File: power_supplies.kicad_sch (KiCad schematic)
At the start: 47 parts, among them IC1 ECP5-BGA256, U15 1V8REG, U3 3V3REG, U4 1V15REG, U5 2V5REG

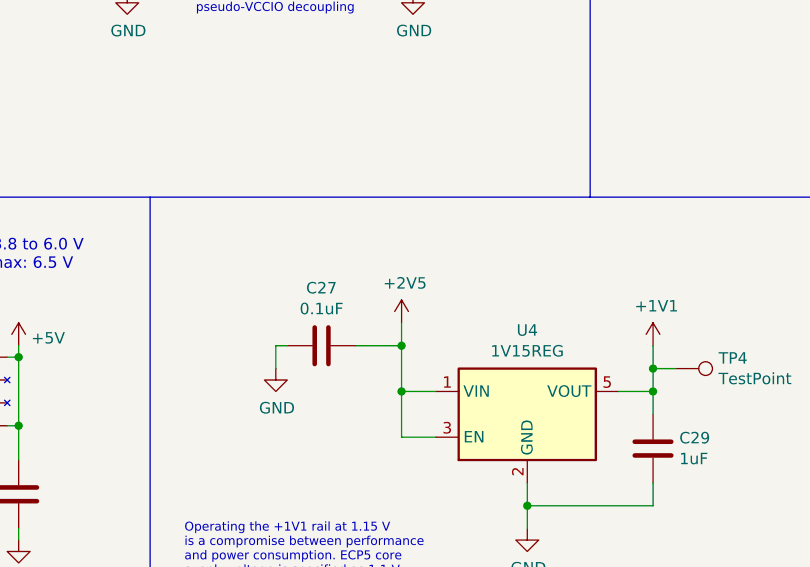
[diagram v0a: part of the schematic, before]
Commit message: Connect U4 +1V1 regulator input to +3V3, not +2V5
The FPGA can drive outputs unexpectedly during power supply ramp-up and
ramp-down. The +2V5 regulator starts abruptly when +3V3 approaches 2 V
and starts more slowly with +1V1 chained from it. With +1V1 chained from
+3V3 instead of from +2V5, both +1V1 and +2V5 supplies start up faster,
minimizing the duration of FPGA output glitches. This reduces the
duration of the glitch that causes #9.
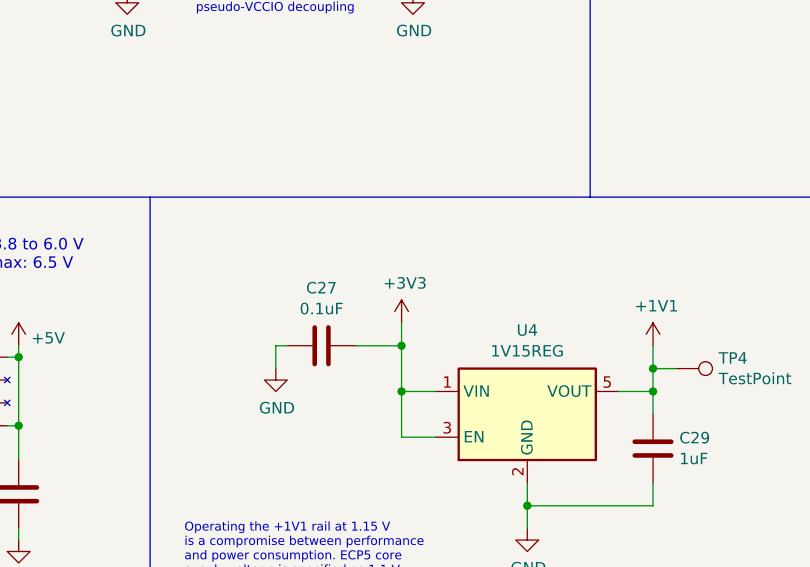
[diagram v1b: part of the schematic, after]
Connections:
- net +2V5: no longer C27.1, U4.1 (VIN), U4.3 (EN)
- net +3V3: now also C27.1, U4.1 (VIN), U4.3 (EN)
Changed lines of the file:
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@@
     (pin "2")
-  )
-  (symbol (lib_id "power:+2V5") (at 121.92 92.71 0) (unit 1)
-    (in_bom yes) (on_board yes)
-    (property "Reference" "#PWR030" (id 0) (at 121.92 96.52 0)
-      (effects (font (size 1.27 1.27)) hide)
-    )
-    (property "Value" "+2V5" (id 1) (at 122.301 88.3158 0))
-    (property "Footprint" "" (id 2) (at 121.92 92.71 0)
-      (effects (font (size 1.27 1.27)) hide)
-    )
-    (property "Datasheet" "" (id 3) (at 121.92 92.71 0)
-      (effects (font (size 1.27 1.27)) hide)
-    )
-    (pin "1")
   )
   (symbol (lib_id "power:+1V1") (at 149.86 95.25 0) (unit 1)
@@
     (pin "2")
   )
+  (symbol (lib_id "power:+3V3") (at 121.92 92.71 0) (unit 1)
+    (in_bom yes) (on_board yes)
+    (property "Reference" "#PWR030" (id 0) (at 121.92 96.52 0)
+      (effects (font (size 1.27 1.27)) hide)
+    )
+    (property "Value" "+3V3" (id 1) (at 122.301 88.3158 0))
+    (property "Footprint" "" (id 2) (at 121.92 92.71 0)
+      (effects (font (size 1.27 1.27)) hide)
+    )
+    (property "Datasheet" "" (id 3) (at 121.92 92.71 0)
+      (effects (font (size 1.27 1.27)) hide)
+    )
+    (pin "1")
+  )
   (symbol (lib_id "Device:R") (at 55.245 149.86 90) (unit 1)

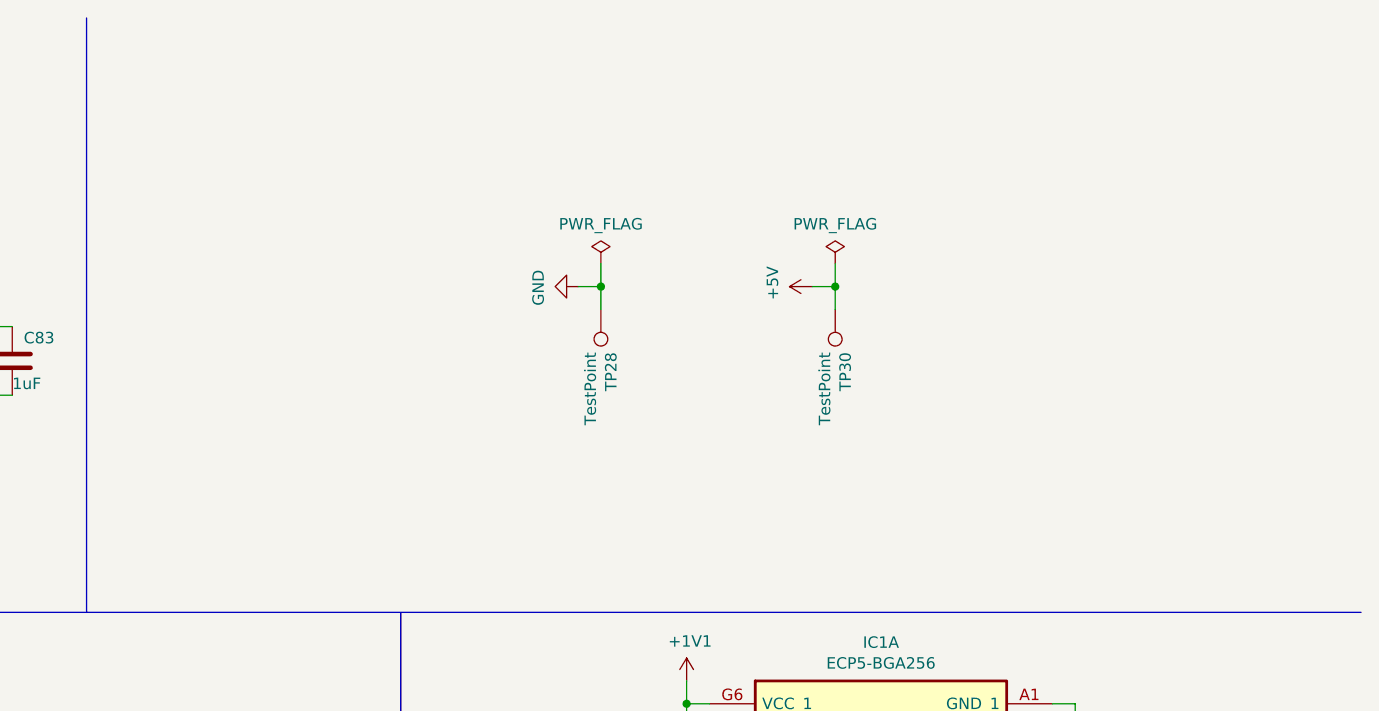
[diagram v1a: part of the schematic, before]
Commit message: Add POWER_GOOD signal
This open collector signal is driven low to indicate that +3V3 is at a
voltage high enough for the FPGA to operate normally. It is used to gate
power input and power passthrough control outputs from the FPGA.

Fixes #9
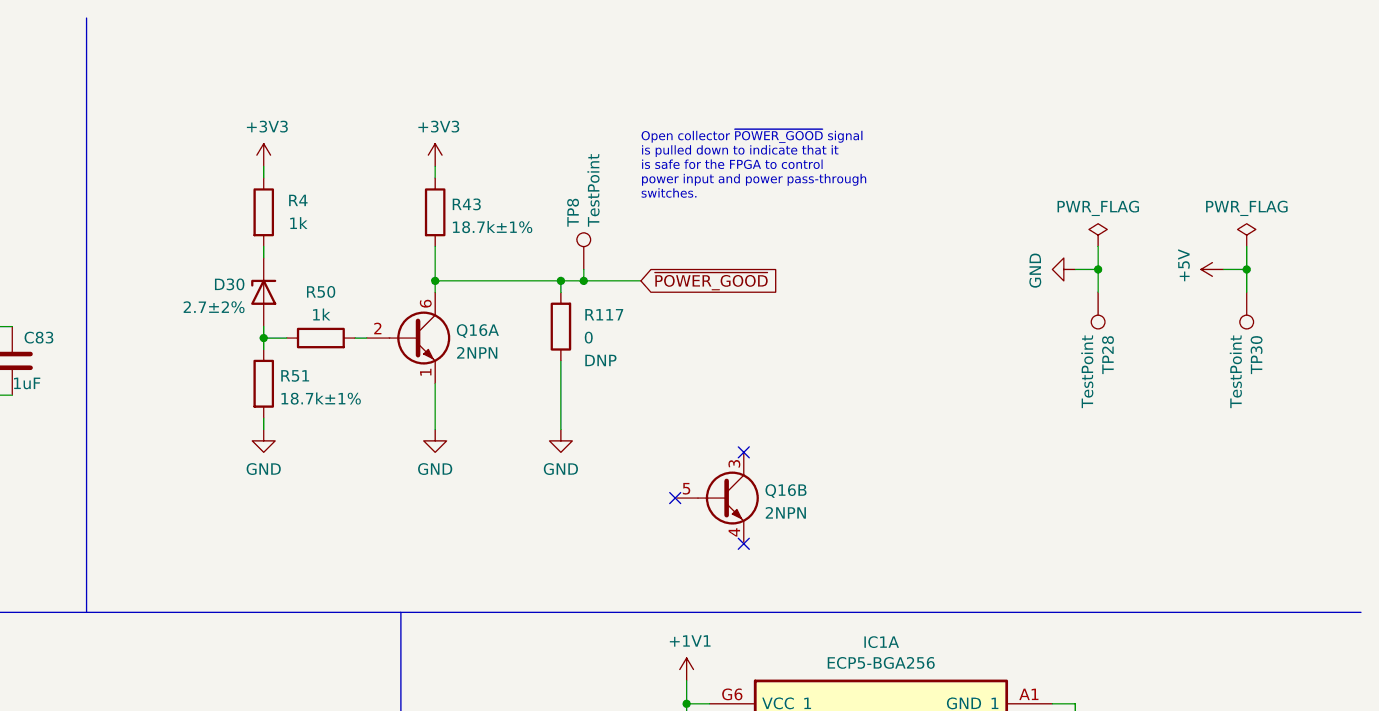
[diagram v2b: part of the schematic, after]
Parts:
- added D30: 2.7±2%, cynthion:DFN1006-2, symbol Device:D_Zener
- added Q16: 2NPN, Package_TO_SOT_SMD:SOT-363_SC-70-6, symbol Transistor_BJT:BC847BS
- added R117: 0, Resistor_SMD:R_0402_1005Metric, symbol Device:R
- added R4, R50: 1k, Resistor_SMD:R_0402_1005Metric, symbol Device:R
- added R43, R51: 18.7k±1%, Resistor_SMD:R_0402_1005Metric, symbol Device:R
- added TP8: TestPoint, TestPoint:TestPoint_Pad_D1.0mm, symbol Connector:TestPoint
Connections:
- net +3V3: now also R4.1, R43.1
- net GND: now also Q16.1 (E1), R117.1, R51.2
- new net: D30.2 (A), R50.1, R51.1
- new net: Q16.2 (B1), R50.2
- new net: D30.1 (K), R4.2
- new net ~{POWER_GOOD}: Q16.6 (C1), R117.2, R43.2, TP8.1
- no-connect marks 0 -> 3
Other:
- note added: "Open collector ~{POWER_GOOD} signal is pulled down to indicate that it is safe for the FPGA to control power input and power pass-through switches."
- moved on the sheet: TP28, TP30

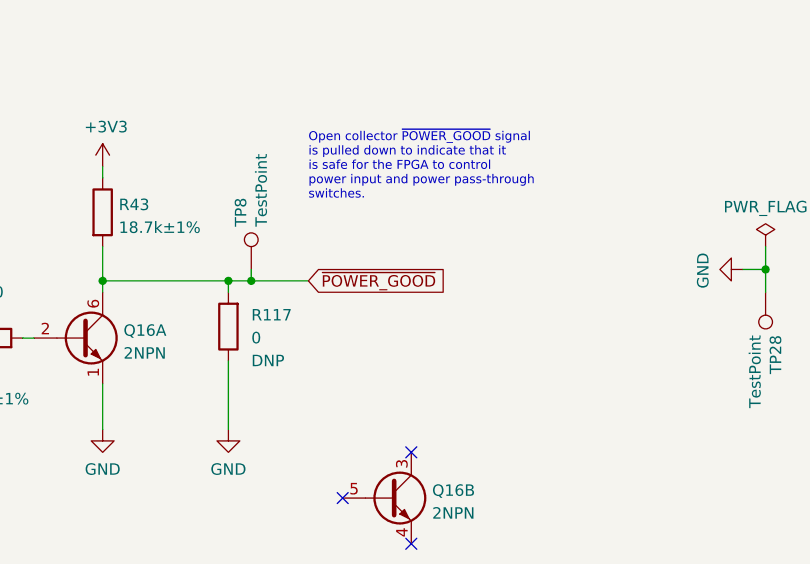
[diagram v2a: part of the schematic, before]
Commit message: Rearrange schematic for readability
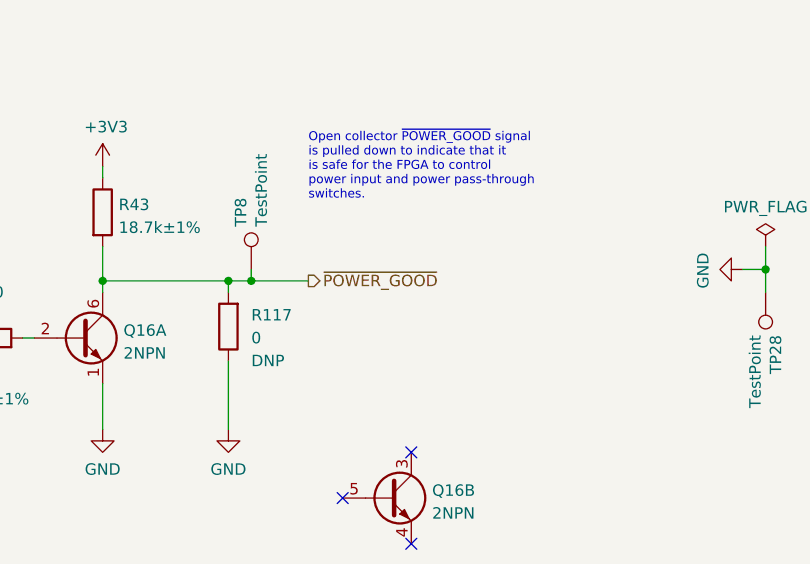
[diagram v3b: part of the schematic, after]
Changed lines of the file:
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@@
     (effects (font (size 0.9906 0.9906)) (justify left bottom))
   )
-  (global_label "~{POWER_GOOD}" (shape input) (at 204.47 41.91 0) (fields_autoplaced)
+  (hierarchical_label "~{POWER_GOOD}" (shape output) (at 204.47 41.91 0)
     (effects (font (size 1.27 1.27)) (justify left))
-    (property "Intersheet References" "${INTERSHEET_REFS}" (id 0) (at 219.4337 41.9894 0)
-      (effects (font (size 1.27 1.27)) (justify left) hide)
-    )
   )
   (symbol (lib_id "fpgas_and_processors:ECP5-BGA256") (at 212.09 86.36 0) (unit 1)

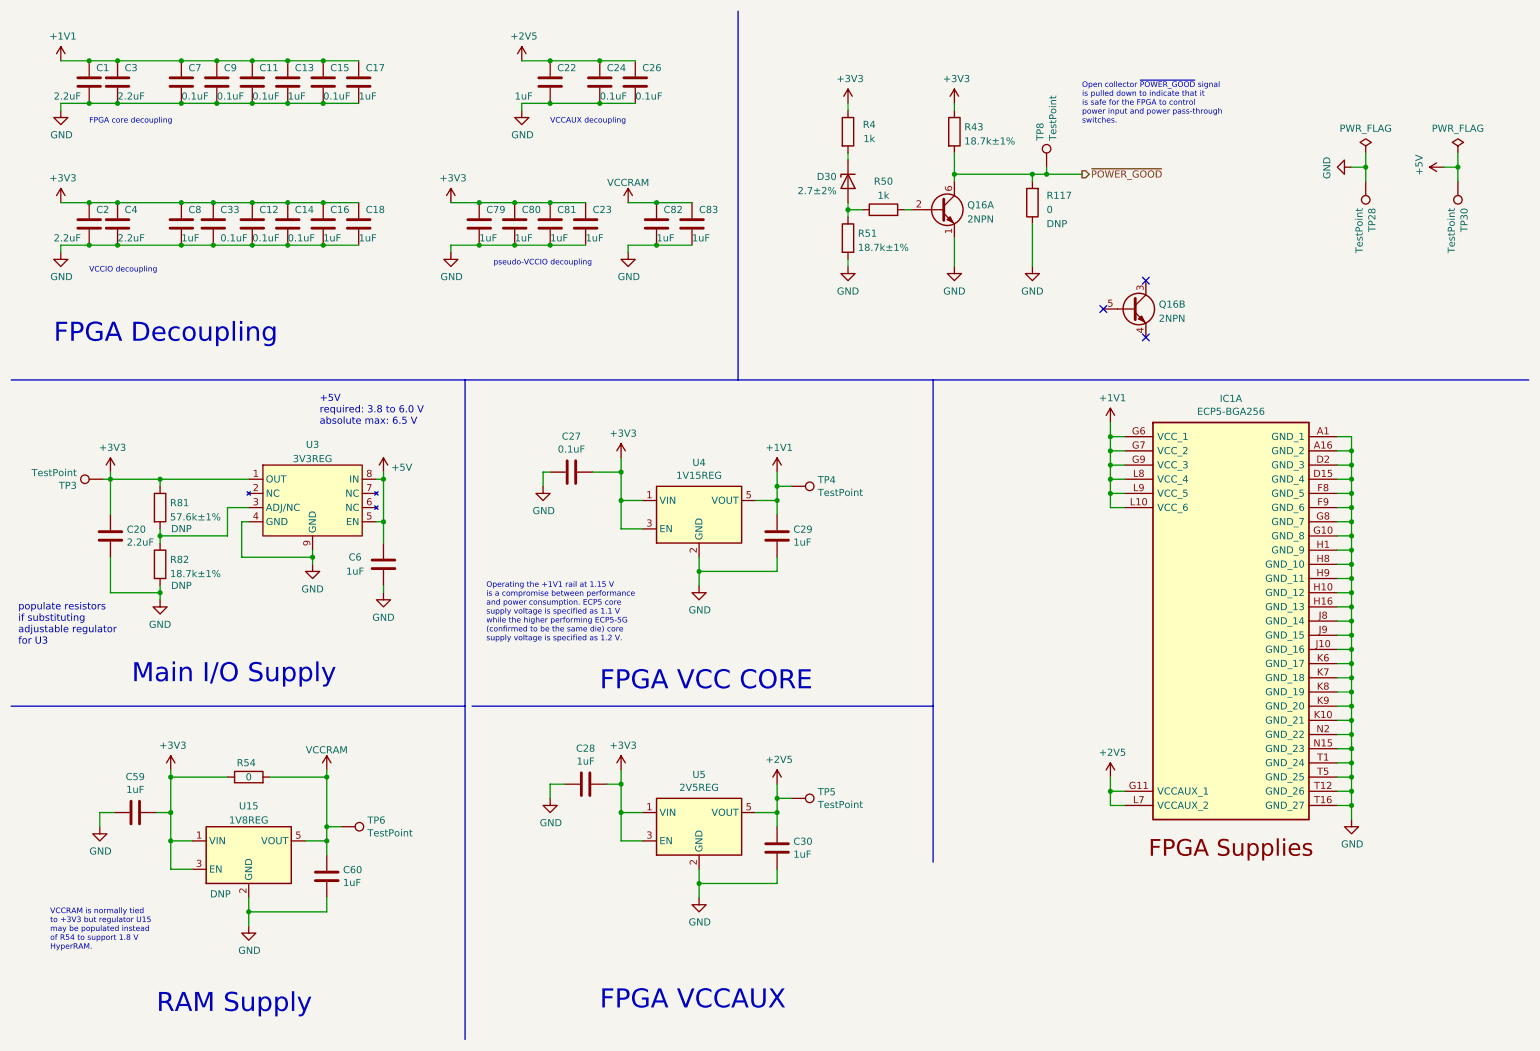
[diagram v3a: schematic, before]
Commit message: Upgrade to KiCad 7
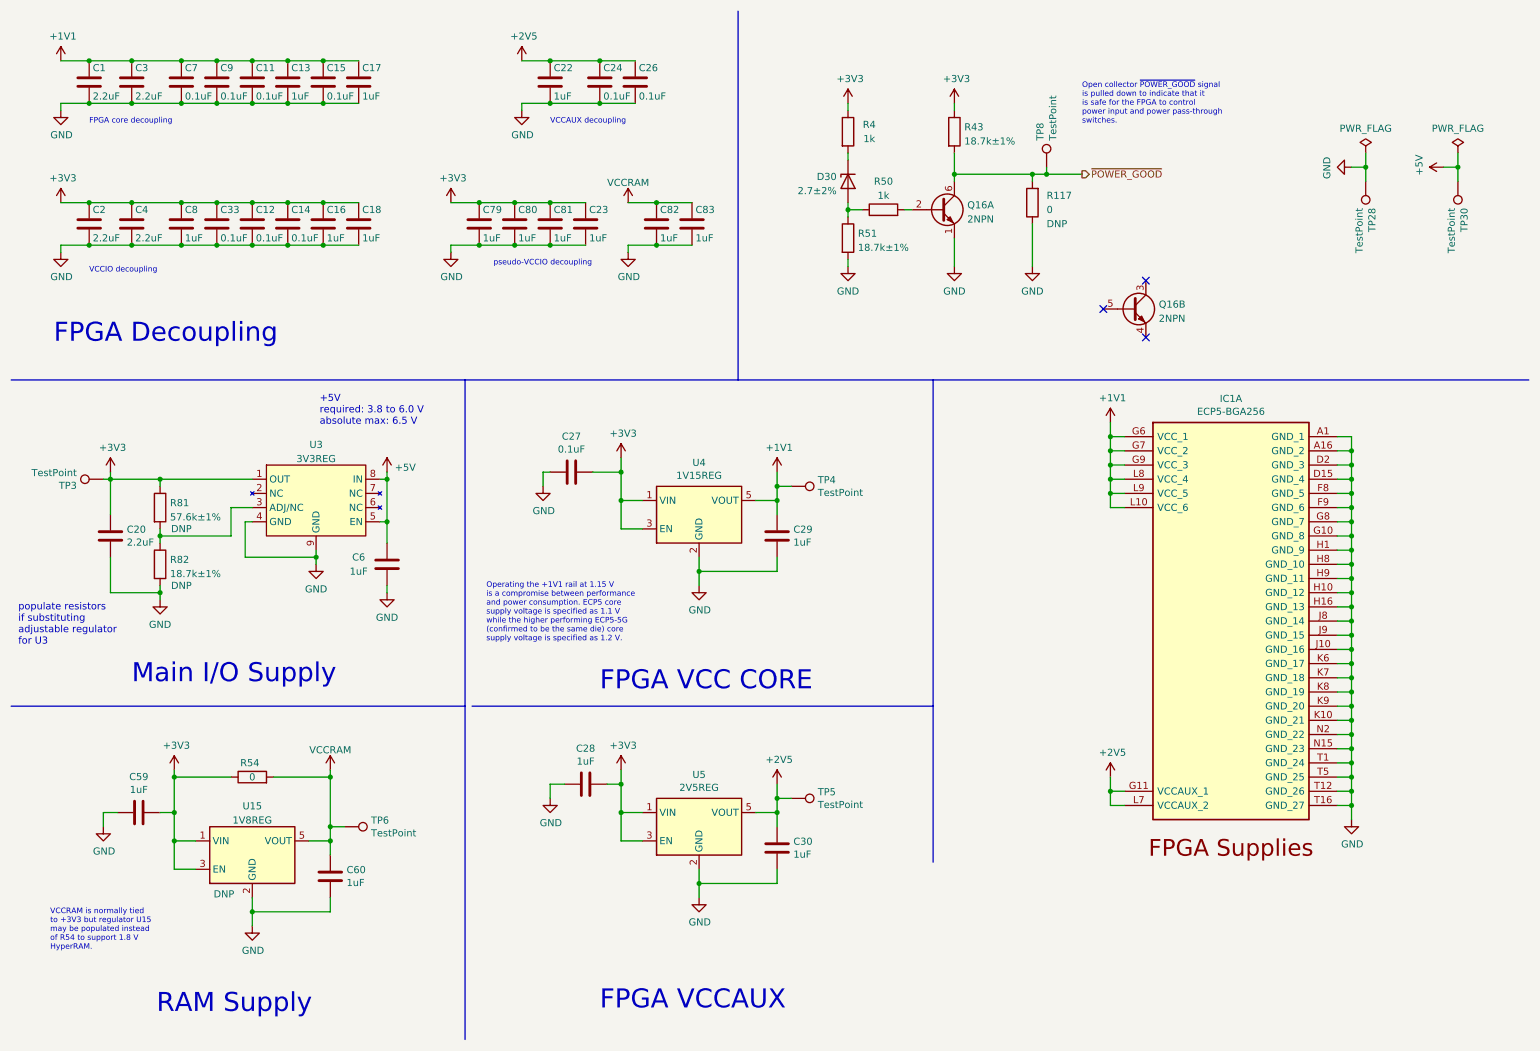
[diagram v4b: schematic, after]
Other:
- moved on the sheet: C3, C33, C4, C59, C6, C60, R54, TP6, U15, U3
